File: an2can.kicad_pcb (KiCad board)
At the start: 2 copper layers, 1 part

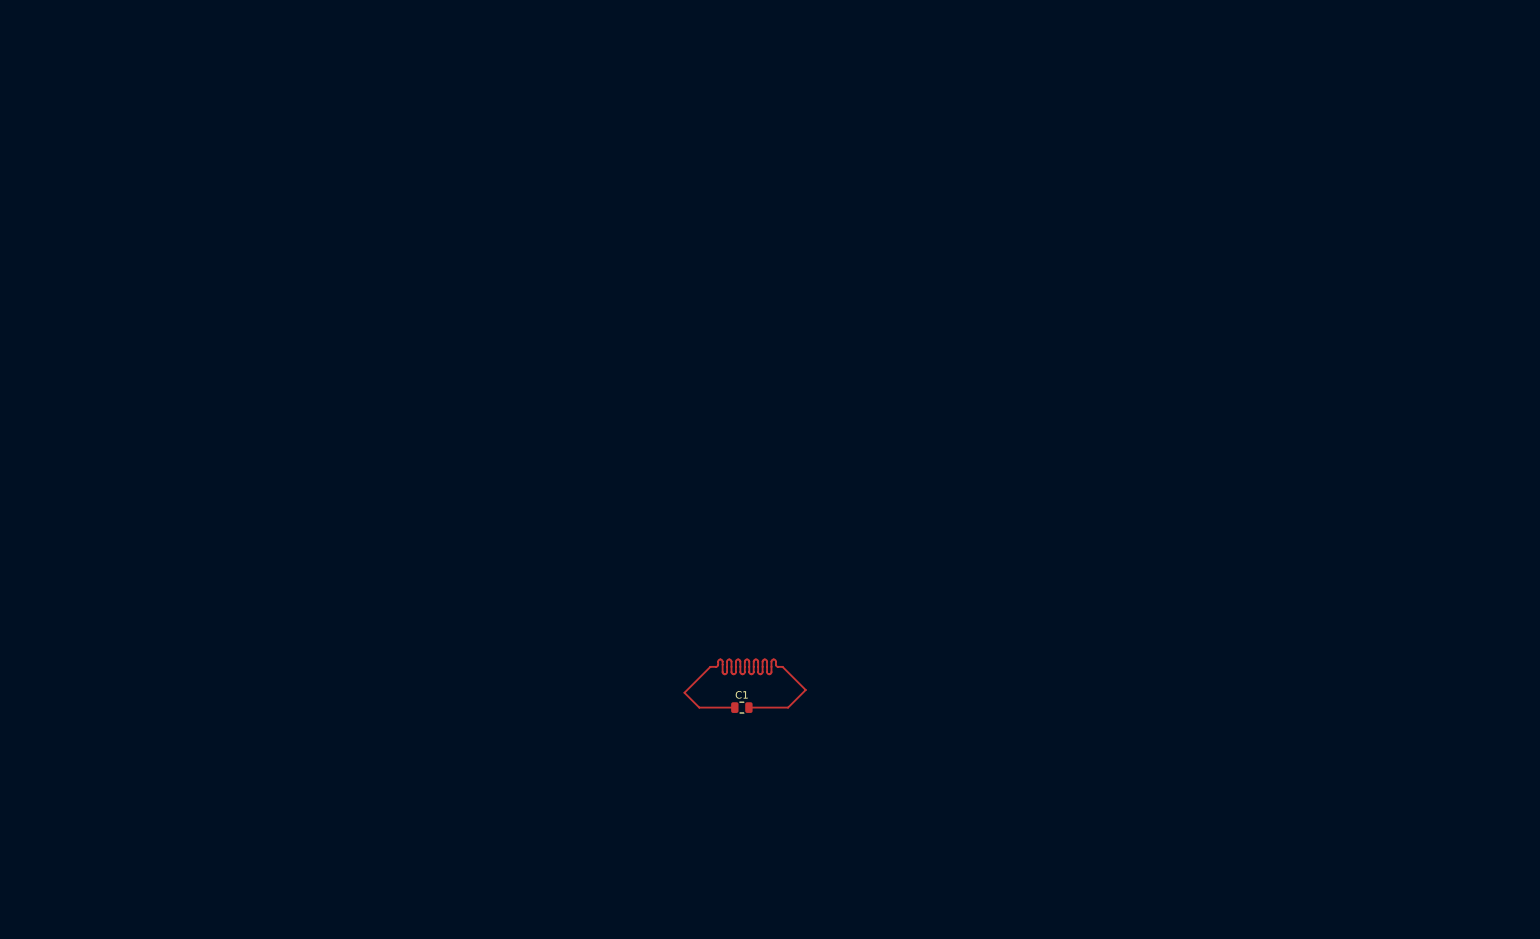
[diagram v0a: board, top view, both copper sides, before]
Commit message: pcb: draft digital section and partial analog
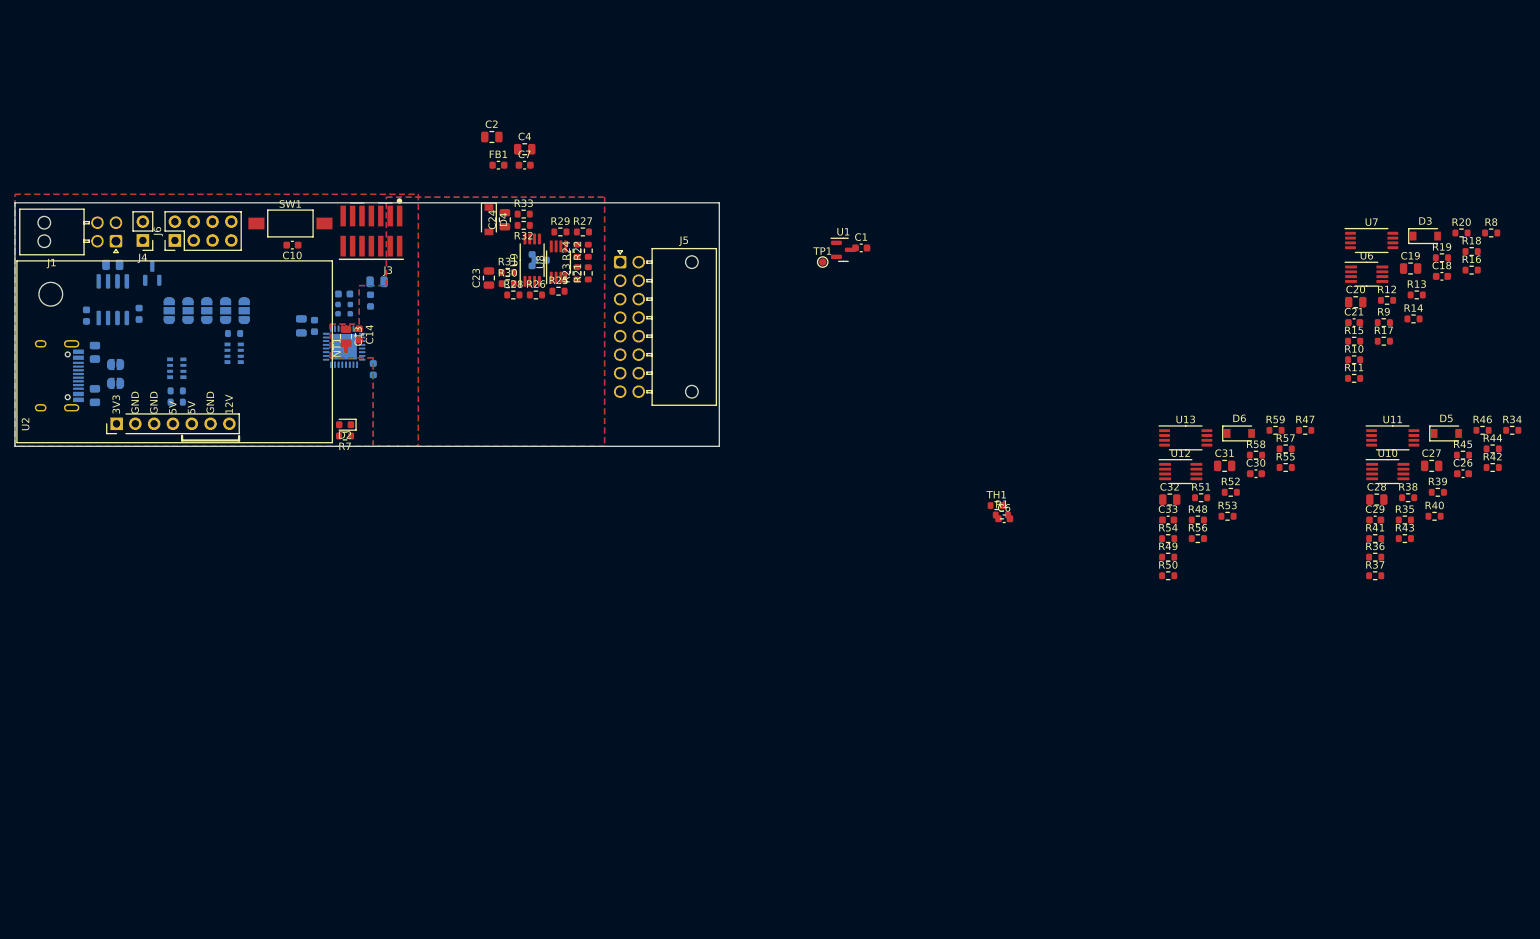
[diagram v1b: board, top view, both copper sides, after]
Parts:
- added C10: 100n, Capacitor_SMD:C_0603_1608Metric, F.Cu at (90.0, 26.3)
- added C11: 100n, Capacitor_SMD:C_0603_1608Metric, B.Cu at (101.0, 43.0)
- added C12: 100n, Capacitor_SMD:C_0603_1608Metric, B.Cu at (97.0, 32.9)
- added C13: 1u, Capacitor_SMD:C_0805_2012Metric, F.Cu at (97.3, 38.6)
- added C14: 100n, Capacitor_SMD:C_0603_1608Metric, F.Cu at (99.1, 38.4)
- added C15: 10u, Capacitor_SMD:C_0805_2012Metric, B.Cu at (91.3, 37.2)
- added C16: 100n, Capacitor_SMD:C_0603_1608Metric, B.Cu at (69.3, 35.6)
- added C17: 100n, Capacitor_SMD:C_0603_1608Metric, B.Cu at (62.2, 35.8)
- added C18: 100n, Capacitor_SMD:C_0603_1608Metric, F.Cu at (245.3, 30.5)
- added C19: C, Capacitor_SMD:C_0805_2012Metric, F.Cu at (241.1, 29.4)
- added C2: C, Capacitor_SMD:C_0805_2012Metric, F.Cu at (117.0, 11.7)
- added C20: C, Capacitor_SMD:C_0805_2012Metric, F.Cu at (233.7, 34.0)
- added C21: 100n, Capacitor_SMD:C_0603_1608Metric, F.Cu at (233.4, 36.8)
- added C22: 100n, Capacitor_SMD:C_0603_1608Metric, B.Cu at (123.6, 28.3)
- added C23: C, Capacitor_SMD:C_0805_2012Metric, F.Cu at (116.6, 30.7)
- added C24: C, Capacitor_SMD:C_0805_2012Metric, F.Cu at (118.7, 22.9)
- added C25: 100n, Capacitor_SMD:C_0603_1608Metric, B.Cu at (122.4, 28.3)
- added C26: 100n, Capacitor_SMD:C_0603_1608Metric, F.Cu at (248.1, 57.2)
- added C27: C, Capacitor_SMD:C_0805_2012Metric, F.Cu at (243.9, 56.1)
- added C28: C, Capacitor_SMD:C_0805_2012Metric, F.Cu at (236.5, 60.7)
- added C29: 100n, Capacitor_SMD:C_0603_1608Metric, F.Cu at (236.3, 63.4)
- added C3: C, Capacitor_SMD:C_0805_2012Metric, B.Cu at (101.5, 31.2)
- added C30: 100n, Capacitor_SMD:C_0603_1608Metric, F.Cu at (220.2, 57.2)
- added C31: C, Capacitor_SMD:C_0805_2012Metric, F.Cu at (216.0, 56.1)
- added C32: C, Capacitor_SMD:C_0805_2012Metric, F.Cu at (208.5, 60.7)
- added C33: 100n, Capacitor_SMD:C_0603_1608Metric, F.Cu at (208.3, 63.4)
- added C4: C, Capacitor_SMD:C_0805_2012Metric, F.Cu at (121.4, 13.3)
- added C6: 100n, Capacitor_SMD:C_0603_1608Metric, F.Cu at (186.2, 63.2)
- added C7: C, Capacitor_SMD:C_0603_1608Metric, F.Cu at (121.4, 15.5)
- added C9: 100n, Capacitor_SMD:C_0603_1608Metric, B.Cu at (93.0, 37.2)
- added D2: USER LED, LED_SMD:LED_0603_1608Metric, F.Cu at (97.2, 50.5)
- added D3: D_Schottky, Diode_SMD:D_SOD-123, F.Cu at (243.1, 25.1)
- added D4: D_Schottky, Diode_SMD:D_SOD-123, F.Cu at (116.6, 22.9)
- added D5: D_Schottky, Diode_SMD:D_SOD-123, F.Cu at (245.9, 51.7)
- added D6: D_Schottky, Diode_SMD:D_SOD-123, F.Cu at (217.9, 51.7)
- added FB1: FerriteBead, Inductor_SMD:L_0603_1608Metric, F.Cu at (117.9, 15.5)
- added FB2: FerriteBead, Inductor_SMD:L_0603_1608Metric, B.Cu at (100.6, 33.8)
- added J1: PWR/CAN, Connector_Molex:Molex_Nano-Fit_105314-xx04_2x02_P2.50mm_Horizontal, F.Cu at (66.2, 25.8)
- added J2: USB C, Connector_USB:USB_C_Receptacle_HRO_TYPE-C-31-M-12, B.Cu at (57.1, 43.9)
- added J3: DBG, Eagle_Connectors:SAMTEC_FTSH-107-01-L-DV-K-TR, F.Cu at (100.7, 24.4)
- added J4: 5V IN, Connector_PinHeader_2.54mm:PinHeader_1x02_P2.54mm_Vertical, F.Cu at (69.8, 25.7)
- added J5: Inputs, Connector_Molex:Molex_Nano-Fit_105314-xx16_2x08_P2.50mm_Horizontal, F.Cu at (134.3, 28.6)
- added J6: Aux, Connector_PinHeader_2.54mm:PinHeader_2x04_P2.54mm_Vertical, F.Cu at (74.2, 25.7)
- added JP1: A0, Jumper:SolderJumper-3_P1.3mm_Open_RoundedPad1.0x1.5mm, B.Cu at (73.4, 35.1)
- added JP2: A1, Jumper:SolderJumper-3_P1.3mm_Open_RoundedPad1.0x1.5mm, B.Cu at (75.9, 35.1)
- added JP3: A2, Jumper:SolderJumper-3_P1.3mm_Open_RoundedPad1.0x1.5mm, B.Cu at (78.5, 35.1)
- added JP4: A3, Jumper:SolderJumper-3_P1.3mm_Open_RoundedPad1.0x1.5mm, B.Cu at (81.0, 35.1)
- added JP5: BOOT0, Jumper:SolderJumper-3_P1.3mm_Open_RoundedPad1.0x1.5mm, B.Cu at (83.5, 35.1)
- added JP6: USB N, Jumper:SolderJumper-2_P1.3mm_Open_RoundedPad1.0x1.5mm, B.Cu at (66.2, 45.0)
- added JP7: USB P, Jumper:SolderJumper-2_P1.3mm_Open_RoundedPad1.0x1.5mm, B.Cu at (66.2, 42.4)
- added NT1: Net Tie, NetTie:NetTie-2_SMD_Pad0.5mm, F.Cu at (97.3, 40.1)
- added Q1: PMV65XP, Package_TO_SOT_SMD:SOT-23, B.Cu at (71.1, 30.1)
- added R1: R, Resistor_SMD:R_0603_1608Metric, F.Cu at (185.9, 62.7)
- added R10: 120 0.1%, Resistor_SMD:R_0603_1608Metric, F.Cu at (233.4, 41.8)
- added R11: 120 0.1%, Resistor_SMD:R_0603_1608Metric, F.Cu at (233.4, 44.3)
- added R12: 220k 0.1%, Resistor_SMD:R_0603_1608Metric, F.Cu at (237.9, 33.7)
- added R13: R, Resistor_SMD:R_0603_1608Metric, F.Cu at (241.9, 33.0)
- added R14: R, Resistor_SMD:R_0603_1608Metric, F.Cu at (241.5, 36.3)
- added R15: R, Resistor_SMD:R_0603_1608Metric, F.Cu at (233.4, 39.3)
- added R16: R, Resistor_SMD:R_0603_1608Metric, F.Cu at (249.3, 29.7)
- added R17: R, Resistor_SMD:R_0603_1608Metric, F.Cu at (237.5, 39.3)
- added R18: R, Resistor_SMD:R_0603_1608Metric, F.Cu at (249.3, 27.2)
- added R19: R, Resistor_SMD:R_0603_1608Metric, F.Cu at (245.3, 28.0)
- added R2: 5k1, Resistor_SMD:R_0805_2012Metric, B.Cu at (63.4, 40.8)
- added R20: R, Resistor_SMD:R_0603_1608Metric, F.Cu at (247.9, 24.6)
- added R21: 120 0.1%, Resistor_SMD:R_0603_1608Metric, F.Cu at (130.0, 30.1)
- added R22: 120 0.1%, Resistor_SMD:R_0603_1608Metric, F.Cu at (130.0, 27.1)
- added R23: 120 0.1%, Resistor_SMD:R_0603_1608Metric, F.Cu at (128.5, 30.1)
- added R24: 120 0.1%, Resistor_SMD:R_0603_1608Metric, F.Cu at (128.5, 27.1)
- added R25: 220k 0.1%, Resistor_SMD:R_0603_1608Metric, F.Cu at (126.0, 32.5)
- added R26: R, Resistor_SMD:R_0603_1608Metric, F.Cu at (122.9, 33.0)
- added R27: R, Resistor_SMD:R_0603_1608Metric, F.Cu at (129.3, 24.5)
- added R28: R, Resistor_SMD:R_0603_1608Metric, F.Cu at (119.9, 33.0)
- added R29: R, Resistor_SMD:R_0603_1608Metric, F.Cu at (126.2, 24.5)
- added R3: 5k1, Resistor_SMD:R_0805_2012Metric, B.Cu at (63.4, 46.6)
- added R30: R, Resistor_SMD:R_0603_1608Metric, F.Cu at (119.1, 31.5)
- added R31: R, Resistor_SMD:R_0603_1608Metric, F.Cu at (119.1, 30.0)
- added R32: R, Resistor_SMD:R_0603_1608Metric, F.Cu at (121.3, 23.6)
- added R33: R, Resistor_SMD:R_0603_1608Metric, F.Cu at (121.3, 22.1)
- added R34: 120 0.1%, Resistor_SMD:R_0603_1608Metric, F.Cu at (254.8, 51.3)
- added R35: 120 0.1%, Resistor_SMD:R_0603_1608Metric, F.Cu at (240.3, 63.4)
- added R36: 120 0.1%, Resistor_SMD:R_0603_1608Metric, F.Cu at (236.3, 68.4)
- added R37: 120 0.1%, Resistor_SMD:R_0603_1608Metric, F.Cu at (236.3, 70.9)
- added R38: 220k 0.1%, Resistor_SMD:R_0603_1608Metric, F.Cu at (240.7, 60.4)
- added R39: R, Resistor_SMD:R_0603_1608Metric, F.Cu at (244.7, 59.7)
- added R4: R, Resistor_SMD:R_0603_1608Metric, B.Cu at (74.4, 47.5)
- added R40: R, Resistor_SMD:R_0603_1608Metric, F.Cu at (244.3, 62.9)
- added R41: R, Resistor_SMD:R_0603_1608Metric, F.Cu at (236.3, 65.9)
- added R42: R, Resistor_SMD:R_0603_1608Metric, F.Cu at (252.2, 56.3)
- added R43: R, Resistor_SMD:R_0603_1608Metric, F.Cu at (240.3, 65.9)
- added R44: R, Resistor_SMD:R_0603_1608Metric, F.Cu at (252.2, 53.8)
- added R45: R, Resistor_SMD:R_0603_1608Metric, F.Cu at (248.1, 54.7)
- added R46: R, Resistor_SMD:R_0603_1608Metric, F.Cu at (250.8, 51.3)
- added R47: 120 0.1%, Resistor_SMD:R_0603_1608Metric, F.Cu at (226.8, 51.3)
- added R48: 120 0.1%, Resistor_SMD:R_0603_1608Metric, F.Cu at (212.3, 63.4)
- added R49: 120 0.1%, Resistor_SMD:R_0603_1608Metric, F.Cu at (208.3, 68.4)
- added R5: R, Resistor_SMD:R_0603_1608Metric, B.Cu at (74.4, 46.0)
- added R50: 120 0.1%, Resistor_SMD:R_0603_1608Metric, F.Cu at (208.3, 70.9)
- added R51: 220k 0.1%, Resistor_SMD:R_0603_1608Metric, F.Cu at (212.8, 60.4)
- added R52: R, Resistor_SMD:R_0603_1608Metric, F.Cu at (216.8, 59.7)
- added R53: R, Resistor_SMD:R_0603_1608Metric, F.Cu at (216.3, 62.9)
- added R54: R, Resistor_SMD:R_0603_1608Metric, F.Cu at (208.3, 65.9)
- added R55: R, Resistor_SMD:R_0603_1608Metric, F.Cu at (224.2, 56.3)
- added R56: R, Resistor_SMD:R_0603_1608Metric, F.Cu at (212.3, 65.9)
- added R57: R, Resistor_SMD:R_0603_1608Metric, F.Cu at (224.2, 53.8)
- added R58: R, Resistor_SMD:R_0603_1608Metric, F.Cu at (220.2, 54.7)
- added R59: R, Resistor_SMD:R_0603_1608Metric, F.Cu at (222.8, 51.3)
- added R6: 120, Resistor_SMD:R_0805_2012Metric, B.Cu at (65.8, 29.0)
- added R60: R, Resistor_SMD:R_0603_1608Metric, B.Cu at (82.2, 38.2)
- added R7: 1k, Resistor_SMD:R_0603_1608Metric, F.Cu at (97.2, 52.1)
- added R8: 120 0.1%, Resistor_SMD:R_0603_1608Metric, F.Cu at (252.0, 24.6)
- added R9: 120 0.1%, Resistor_SMD:R_0603_1608Metric, F.Cu at (237.5, 36.8)
- added RN1: R, Resistor_SMD:R_Array_Convex_4x0603, B.Cu at (82.2, 40.9)
- added RN2: R, Resistor_SMD:R_Array_Convex_4x0603, B.Cu at (74.4, 42.9)
- added SW1: RESET, Button_Switch_SMD:SW_SPST_FSMSM, F.Cu at (89.8, 23.4)
- added TH1: Thermistor, Resistor_SMD:R_0603_1608Metric, F.Cu at (185.2, 61.5)
- added TP1: Offset, TestPoint:TestPoint_Pad_D1.0mm, F.Cu at (161.7, 28.6)
- added U1: MAX6025, Package_TO_SOT_SMD:SOT-23, F.Cu at (164.5, 26.9)
- added U10: AD8221ARZ, Package_SO:MSOP-8_3x3mm_P0.65mm, F.Cu at (238.0, 56.9)
- added U11: Opamp_Dual, Package_SO:TSSOP-8_4.4x3mm_P0.65mm, F.Cu at (238.7, 52.3)
- added U12: AD8221ARZ, Package_SO:MSOP-8_3x3mm_P0.65mm, F.Cu at (210.0, 56.9)
- added U13: Opamp_Dual, Package_SO:TSSOP-8_4.4x3mm_P0.65mm, F.Cu at (210.7, 52.3)
- added U2: Tex_DCDC_v2, Eagle_Main:Tex_DCDC_v2_horizontal, F.Cu at (66.3, 50.4)
- added U3: DSC61XX, Package_LGA:VLGA-4_2x2.5mm_P1.65mm, B.Cu at (97.0, 34.9)
- added U4: STM32L432KCUx, Package_DFN_QFN:QFN-32-1EP_5x5mm_P0.5mm_EP3.45x3.45mm, B.Cu at (97.0, 40.0)
- added U5: MCP2562FD, Package_SO:SOIC-8_3.9x4.9mm_P1.27mm, B.Cu at (65.8, 33.7)
- added U6: AD8221ARZ, Package_SO:MSOP-8_3x3mm_P0.65mm, F.Cu at (235.1, 30.2)
- added U7: Opamp_Dual, Package_SO:TSSOP-8_4.4x3mm_P0.65mm, F.Cu at (235.8, 25.7)
- added U8: AD8221ARZ, Package_SO:MSOP-8_3x3mm_P0.65mm, F.Cu at (126.0, 28.6)
- added U9: Opamp_Dual, Package_SO:TSSOP-8_4.4x3mm_P0.65mm, F.Cu at (122.4, 28.3)
- C1: value 1F -> 100n; footprint Capacitor_SMD:C_0805_2012Metric -> Capacitor_SMD:C_0603_1608Metric
- moved C1 64.1 mm to (166.9, 26.7)
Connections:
- C1 pad 1: Net-(C1-Pad1) -> GNDA
- C1 pad 2: Net-(C1-Pad1) -> /2V5_OFFSET
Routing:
- net Net-(C1-Pad1): track 57.5 -> 0.00 mm
- added copper zone on B.Cu, net GND
- added copper zone on F.Cu, net GND
- added copper zone on B.Cu, net GNDA
- added copper zone on F.Cu, net GNDA
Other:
- board outline added: 95.1 x 32.9 mm

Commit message: pcb: full draft of positioning
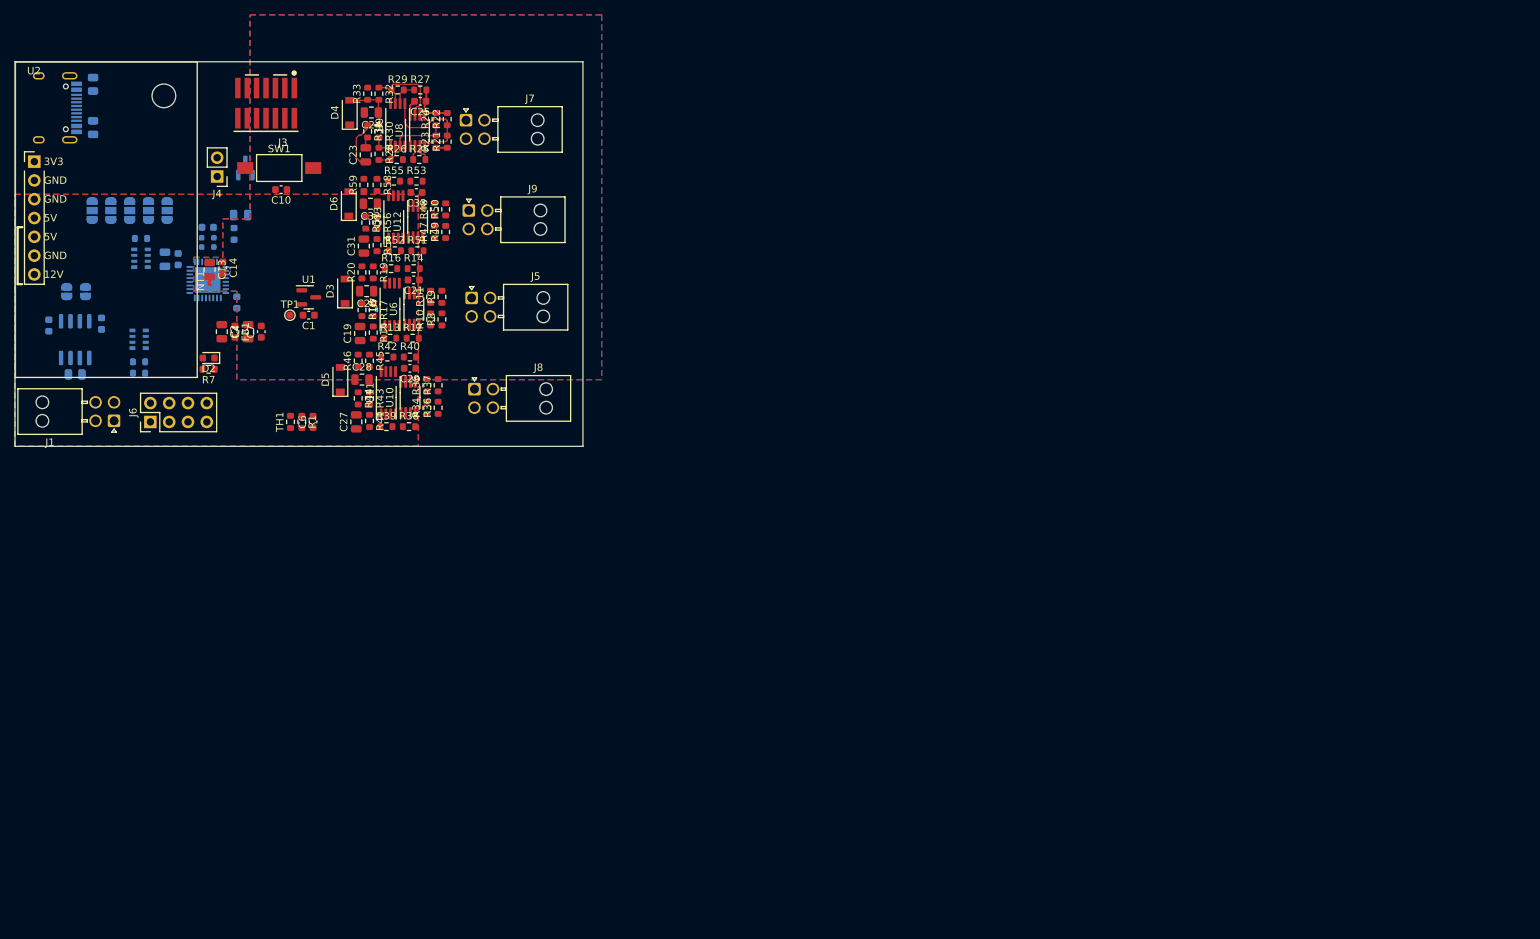
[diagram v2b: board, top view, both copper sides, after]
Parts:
- removed C18, C22, C26, C30: 100n, Capacitor_SMD:C_0603_1608Metric
- added J7: Input, Connector_Molex:Molex_Nano-Fit_105314-xx04_2x02_P2.50mm_Horizontal, F.Cu at (113.5, 9.42)
- added J8: Input, Connector_Molex:Molex_Nano-Fit_105314-xx04_2x02_P2.50mm_Horizontal, F.Cu at (114.6, 45.7)
- added J9: Input, Connector_Molex:Molex_Nano-Fit_105314-xx04_2x02_P2.50mm_Horizontal, F.Cu at (113.9, 21.6)
- C25: moved to F.Cu
- J5: value Inputs -> Input; footprint Connector_Molex:Molex_Nano-Fit_105314-xx16_2x08_P2.50mm_Horizontal -> Connector_Molex:Molex_Nano-Fit_105314-xx04_2x02_P2.50mm_Horizontal
- moved R44 153.4 mm to (98.9, 47.0), turned to -90 degrees
- moved R46 152.1 mm to (98.9, 41.9), turned to 90 degrees
- moved R18 150.1 mm to (99.4, 35.1), turned to -90 degrees
- moved R42 150.0 mm to (102.9, 41.4)
- moved D5 149.6 mm to (96.5, 44.5), turned to 90 degrees
- moved R20 148.6 mm to (99.4, 30.0), turned to 90 degrees
- moved R45 148.2 mm to (100.5, 41.9), turned to -90 degrees
- moved R34 146.6 mm to (108.2, 48.3), turned to 90 degrees
- moved D3 146.1 mm to (97.2, 32.5), turned to 90 degrees
- moved R16 145.9 mm to (103.4, 29.5)
- moved C27 145.4 mm to (98.7, 50.2), turned to 90 degrees
- moved R19 144.4 mm to (101.0, 30.0), turned to -90 degrees
- moved R39 142.3 mm to (102.7, 50.8)
- moved R8 142.2 mm to (110.2, 36.3), turned to 90 degrees
- moved C19 142.2 mm to (99.2, 38.2), turned to 90 degrees
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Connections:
- J5 pad 1: /IN0 -> /Input Stage 2/IN_0+
- J5 pad 2: /IN1 -> /Input Stage 2/IN_1+
- J5 pad 3: /IN2 -> +5VA
- J5 pad 4: /IN3 -> GNDA
- R10 pad 2: /IN3 -> /Input Stage 2/IN_1+
- R11 pad 1: /IN3 -> /Input Stage 2/IN_1+
- R21 pad 2: /IN0 -> /Input Stage 1/IN_0+
- R22 pad 1: /IN0 -> /Input Stage 1/IN_0+
- R23 pad 2: /IN1 -> /Input Stage 1/IN_1+
- R24 pad 1: /IN1 -> /Input Stage 1/IN_1+
- R34 pad 2: /IN4 -> /Input Stage 3/IN_0+
- R35 pad 1: /IN4 -> /Input Stage 3/IN_0+
- R36 pad 2: /IN5 -> /Input Stage 3/IN_1+
- R37 pad 1: /IN5 -> /Input Stage 3/IN_1+
- R47 pad 2: /IN6 -> /Input Stage 4/IN_0+
- R48 pad 1: /IN6 -> /Input Stage 4/IN_0+
- R49 pad 2: /IN7 -> /Input Stage 4/IN_1+
- R50 pad 1: /IN7 -> /Input Stage 4/IN_1+
- R8 pad 2: /IN2 -> /Input Stage 2/IN_0+
- R9 pad 1: /IN2 -> /Input Stage 2/IN_0+
- U10 pad 1: /IN5 -> /Input Stage 3/IN_1+
- U10 pad 4: /IN4 -> /Input Stage 3/IN_0+
- U11 pad 3: /IN5 -> /Input Stage 3/IN_1+
- U11 pad 5: /IN4 -> /Input Stage 3/IN_0+
- U12 pad 1: /IN7 -> /Input Stage 4/IN_1+
- U12 pad 4: /IN6 -> /Input Stage 4/IN_0+
- U13 pad 3: /IN7 -> /Input Stage 4/IN_1+
- U13 pad 5: /IN6 -> /Input Stage 4/IN_0+
- U6 pad 1: /IN3 -> /Input Stage 2/IN_1+
- U6 pad 4: /IN2 -> /Input Stage 2/IN_0+
- U7 pad 3: /IN3 -> /Input Stage 2/IN_1+
- U7 pad 5: /IN2 -> /Input Stage 2/IN_0+
- U8 pad 1: /IN1 -> /Input Stage 1/IN_1+
- U8 pad 4: /IN0 -> /Input Stage 1/IN_0+
- U9 pad 3: /IN1 -> /Input Stage 1/IN_1+
- U9 pad 5: /IN0 -> /Input Stage 1/IN_0+
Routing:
- net /Input Stage 1/IN_0+: track 0.00 -> 15.2 mm
- net /Input Stage 1/OUT_COM_UNFLT: track 0.00 -> 12.7 mm
- net /Input Stage 1/IN_1+: track 0.00 -> 8.85 mm
- net /Input Stage 1/OUT_SINGLE: track 0.00 -> 8.19 mm
- net GNDA: track 0.00 -> 7.89 mm
- net /Input Stage 1/OUT_COM: track 0.00 -> 5.71 mm
- net /Input Stage 1/IN_1-: track 0.00 -> 3.71 mm
- net +5VA: track 0.00 -> 3.59 mm
- net /Input Stage 1/IN_0-: track 0.00 -> 3.44 mm
- net /Input Stage 1/OUT_SINGLE_UNFLT: track 0.00 -> 2.91 mm
- net /Input Stage 1/RG2: track 0.00 -> 2.35 mm
- net /Input Stage 1/RG1: track 0.00 -> 1.93 mm
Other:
- board size 95.1 x 32.9 mm -> 76.7 x 51.9 mm
